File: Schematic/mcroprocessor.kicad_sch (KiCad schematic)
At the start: 17 parts, among them J1 Conn_01x05_Pin, J3 DEBUG_HEADER, SW1 RESET, U1 MAX7375AXR805, U1 STM32F091RCT6

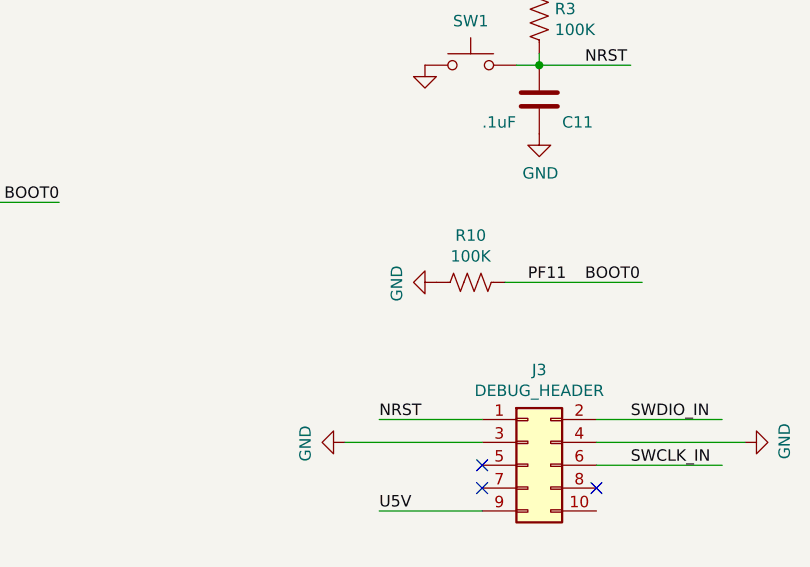
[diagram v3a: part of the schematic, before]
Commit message: fixed LM385 not having voltage div, and ploted plots.
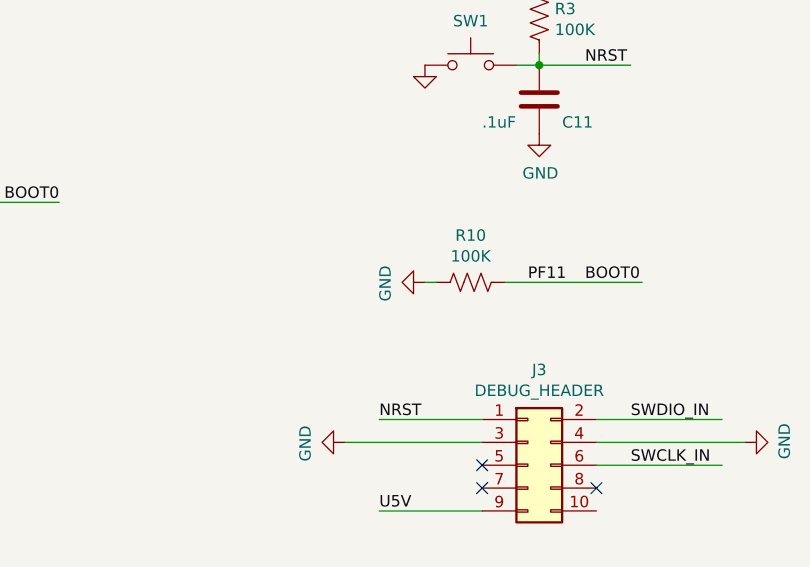
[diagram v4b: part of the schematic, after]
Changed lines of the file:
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@@
+    (stroke (width 0) (type default))
+  )
+  (wire (pts (xy 215.9 55.88) (xy 217.17 55.88))
     (stroke (width 0) (type default))
   )
@@
     )
   )
-  (symbol (lib_id "power:GND") (at 217.17 55.88 270) (unit 1)
-    (in_bom yes) (on_board yes) (dnp no)
-    (property "Reference" "#PWR0130" (at 210.82 55.88 0)
-      (effects (font (size 1.27 1.27)) hide)
-    )
-    (property "Value" "GND" (at 212.7758 56.007 0)
-      (effects (font (size 1.27 1.27)))
-    )
-    (property "Footprint" "" (at 217.17 55.88 0)
-      (effects (font (size 1.27 1.27)) hide)
-    )
-    (property "Datasheet" "" (at 217.17 55.88 0)
-      (effects (font (size 1.27 1.27)) hide)
-    )
+  (symbol (lib_id "power:GND") (at 215.9 55.88 270) (unit 1)
+    (in_bom yes) (on_board yes) (dnp no)
+    (property "Reference" "#PWR0130" (at 209.55 55.88 0)
+      (effects (font (size 1.27 1.27)) hide)
+    )
+    (property "Value" "GND" (at 211.5058 56.007 0)
+      (effects (font (size 1.27 1.27)))
+    )
+    (property "Footprint" "" (at 215.9 55.88 0)
+      (effects (font (size 1.27 1.27)) hide)
+    )
+    (property "Datasheet" "" (at 215.9 55.88 0)
+      (effects (font (size 1.27 1.27)) hide)
+    )
